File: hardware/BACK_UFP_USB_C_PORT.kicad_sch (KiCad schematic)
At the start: 30 parts, among them J7 USB4200-03-A (VIRT FLAG MOUNT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, Q18 PMOS, Q19 PMOS, Q20 PMOS, Q21 PMOS

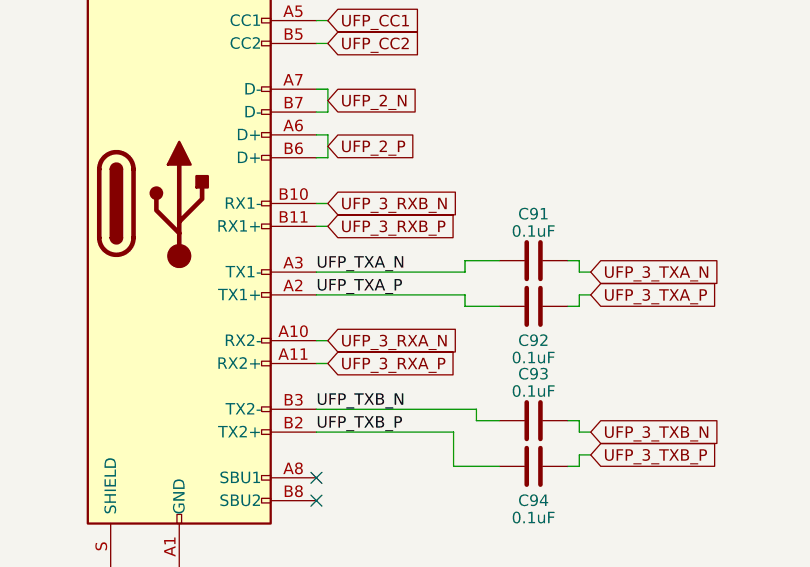
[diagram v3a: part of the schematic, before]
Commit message: working on fixing pcb impeedance
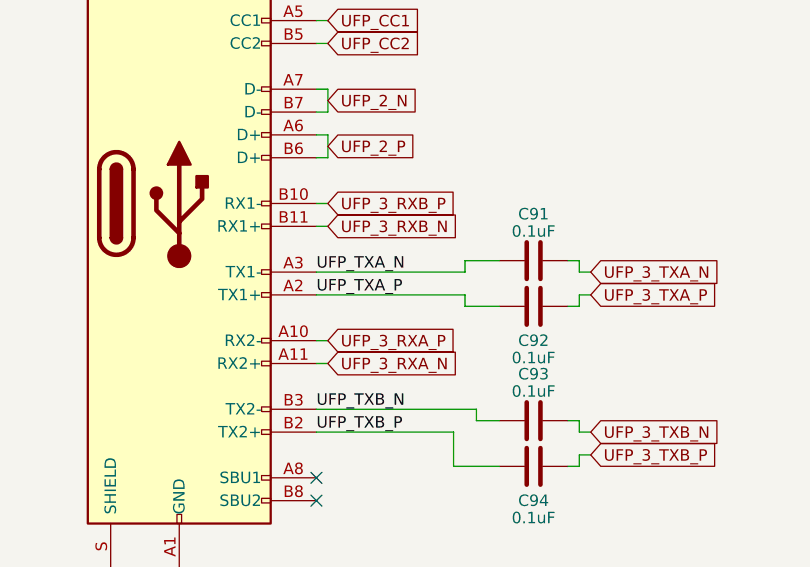
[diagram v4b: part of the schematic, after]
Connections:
- net UFP_3_RXA_N: now also J7.A11 (RX2+); no longer J7.A10 (RX2-)
- net UFP_3_RXA_P: now also J7.A10 (RX2-); no longer J7.A11 (RX2+)
- net UFP_3_RXB_N: now also J7.B11 (RX1+); no longer J7.B10 (RX1-)
- net UFP_3_RXB_P: now also J7.B10 (RX1-); no longer J7.B11 (RX1+)
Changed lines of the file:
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@@
     )
   )
-  (global_label "UFP_3_RXB_N" (shape input) (at 49.53 53.34 0) (fields_autoplaced)
+  (global_label "UFP_3_RXB_N" (shape input) (at 49.53 55.88 0) (fields_autoplaced)
     (effects (font (size 1.27 1.27)) (justify left))
-    (property "Intersheetrefs" "${INTERSHEET_REFS}" (at 65.3172 53.34 0)
+    (property "Intersheetrefs" "${INTERSHEET_REFS}" (at 65.3172 55.88 0)
       (effects (font (size 1.27 1.27)) (justify left) hide)
     )
@@
     )
   )
-  (global_label "UFP_3_RXB_P" (shape input) (at 49.53 55.88 0) (fields_autoplaced)
+  (global_label "UFP_3_RXB_P" (shape input) (at 49.53 53.34 0) (fields_autoplaced)
     (effects (font (size 1.27 1.27)) (justify left))
-    (property "Intersheetrefs" "${INTERSHEET_REFS}" (at 65.2567 55.88 0)
+    (property "Intersheetrefs" "${INTERSHEET_REFS}" (at 65.2567 53.34 0)
       (effects (font (size 1.27 1.27)) (justify left) hide)
     )
@@
     )
   )
-  (global_label "UFP_3_RXA_P" (shape input) (at 49.53 71.12 0) (fields_autoplaced)
+  (global_label "UFP_3_RXA_P" (shape input) (at 49.53 68.58 0) (fields_autoplaced)
     (effects (font (size 1.27 1.27)) (justify left))
-    (property "Intersheetrefs" "${INTERSHEET_REFS}" (at 65.0753 71.12 0)
+    (property "Intersheetrefs" "${INTERSHEET_REFS}" (at 65.0753 68.58 0)
       (effects (font (size 1.27 1.27)) (justify left) hide)
     )
@@
     )
   )
-  (global_label "UFP_3_RXA_N" (shape input) (at 49.53 68.58 0) (fields_autoplaced)
+  (global_label "UFP_3_RXA_N" (shape input) (at 49.53 71.12 0) (fields_autoplaced)
     (effects (font (size 1.27 1.27)) (justify left))
-    (property "Intersheetrefs" "${INTERSHEET_REFS}" (at 65.1358 68.58 0)
+    (property "Intersheetrefs" "${INTERSHEET_REFS}" (at 65.1358 71.12 0)
       (effects (font (size 1.27 1.27)) (justify left) hide)
     )

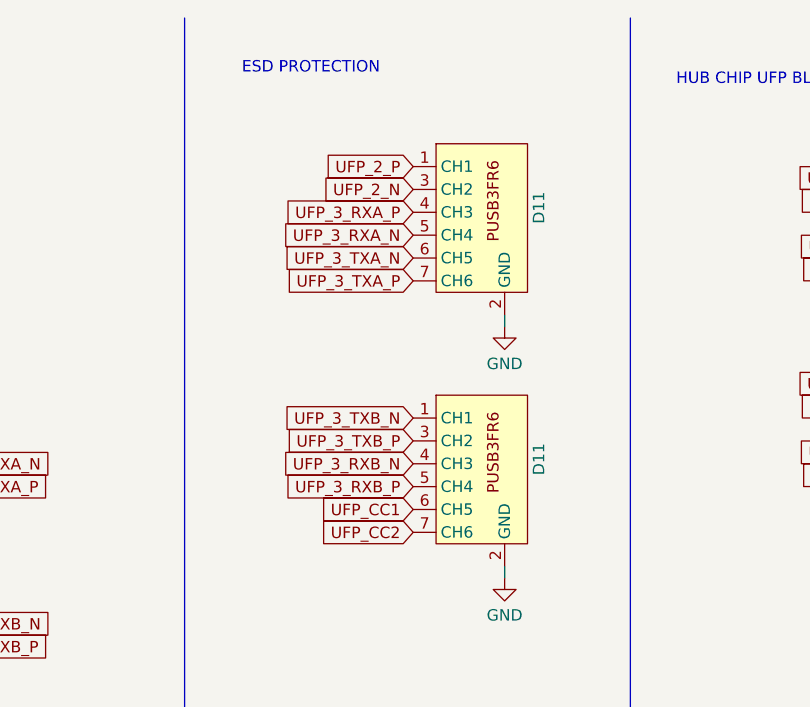
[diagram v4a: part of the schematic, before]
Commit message: fixed DP issues and finneshed overall routeing
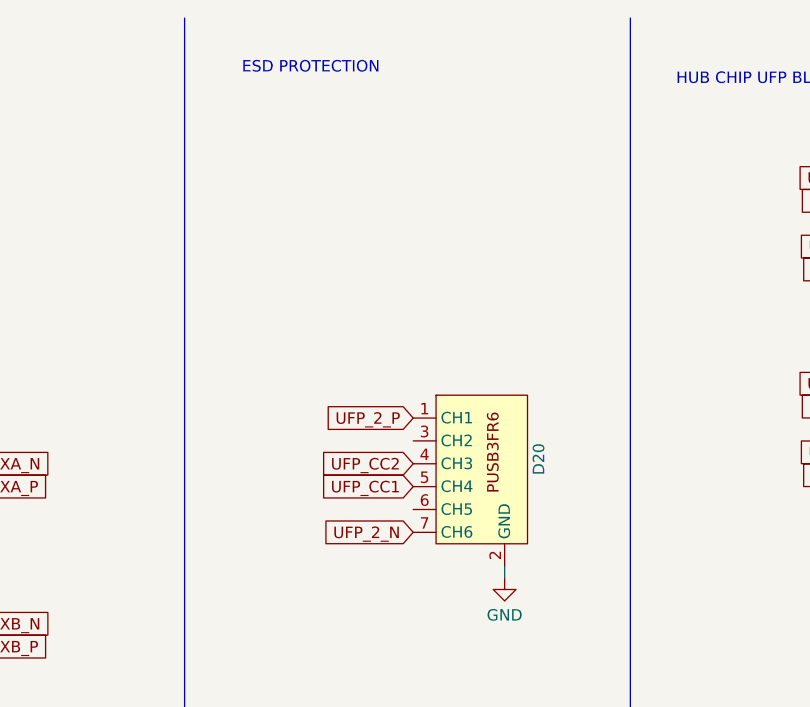
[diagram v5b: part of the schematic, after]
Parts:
- removed D11: ~, CARTHING:PUSB3AB6Z_NEX, symbol CARTHING:PUSB3FR6
- renumbered D11 to D20
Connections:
- net UFP_2_N: now also D20.7 (CH6)
- net UFP_2_P: now also D20.1 (CH1)
- net UFP_3_RXB_N: no longer D20.4 (CH3)
- net UFP_3_RXB_P: no longer D20.5 (CH4)
- net UFP_3_TXB_N: no longer D20.1 (CH1)
- net UFP_3_TXB_P: no longer D20.3 (CH2)
- net UFP_CC1: now also D20.5 (CH4); no longer D20.6 (CH5)
- net UFP_CC2: now also D20.4 (CH3); no longer D20.7 (CH6)
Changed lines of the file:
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@@
-    (stroke (width 0) (type default))
-  )
-  (wire (pts (xy 143.51 44.45) (xy 143.51 45.72))
     (stroke (width 0) (type default))
   )
@@
     (effects (font (size 1.27 1.27)) (justify left bottom))
   )
-  (global_label "UFP_3_TXB_N" (shape input) (at 133.35 55.88 180) (fields_autoplaced)
-    (effects (font (size 1.27 1.27)) (justify right))
-    (property "Intersheetrefs" "${INTERSHEET_REFS}" (at 117.8652 55.88 0)
-      (effects (font (size 1.27 1.27)) (justify right) hide)
-    )
-  )
   (global_label "UFP_2_N" (shape input) (at 49.53 41.91 0) (fields_autoplaced)
     (effects (font (size 1.27 1.27)) (justify left))
@@
     )
   )
-  (global_label "UFP_2_P" (shape input) (at 133.35 27.94 180) (fields_autoplaced)
-    (effects (font (size 1.27 1.27)) (justify right))
-    (property "Intersheetrefs" "${INTERSHEET_REFS}" (at 122.3404 27.94 0)
+  (global_label "UFP_2_P" (shape input) (at 133.35 55.88 180) (fields_autoplaced)
+    (effects (font (size 1.27 1.27)) (justify right))
+    (property "Intersheetrefs" "${INTERSHEET_REFS}" (at 122.3404 55.88 0)
       (effects (font (size 1.27 1.27)) (justify right) hide)
     )
@@
     )
   )
-  (global_label "UFP_2_N" (shape input) (at 133.35 30.48 180) (fields_autoplaced)
-    (effects (font (size 1.27 1.27)) (justify right))
-    (property "Intersheetrefs" "${INTERSHEET_REFS}" (at 122.2799 30.48 0)
+  (global_label "UFP_2_N" (shape input) (at 133.35 68.58 180) (fields_autoplaced)
+    (effects (font (size 1.27 1.27)) (justify right))
+    (property "Intersheetrefs" "${INTERSHEET_REFS}" (at 122.2799 68.58 0)
       (effects (font (size 1.27 1.27)) (justify right) hide)
     )
@@
     )
   )
-  (global_label "UFP_3_TXA_P" (shape input) (at 133.35 40.64 180) (fields_autoplaced)
-    (effects (font (size 1.27 1.27)) (justify right))
-    (property "Intersheetrefs" "${INTERSHEET_REFS}" (at 118.1071 40.64 0)
-      (effects (font (size 1.27 1.27)) (justify right) hide)
-    )
-  )
   (global_label "UFP_3_TXB_N" (shape input) (at 78.74 78.74 0) (fields_autoplaced)
     (effects (font (size 1.27 1.27)) (justify left))
@@
     )
   )
-  (global_label "UFP_3_TXB_P" (shape input) (at 133.35 58.42 180) (fields_autoplaced)
-    (effects (font (size 1.27 1.27)) (justify right))
-    (property "Intersheetrefs" "${INTERSHEET_REFS}" (at 117.9257 58.42 0)
-      (effects (font (size 1.27 1.27)) (justify right) hide)
-    )
-  )
-  (global_label "UFP_3_RXA_P" (shape input) (at 133.35 33.02 180) (fields_autoplaced)
-    (effects (font (size 1.27 1.27)) (justify right))
-    (property "Intersheetrefs" "${INTERSHEET_REFS}" (at 117.8047 33.02 0)
-      (effects (font (size 1.27 1.27)) (justify right) hide)
-    )
-  )
-  (global_label "UFP_CC1" (shape input) (at 133.35 66.04 180) (fields_autoplaced)
-    (effects (font (size 1.27 1.27)) (justify right))
-    (property "Intersheetrefs" "${INTERSHEET_REFS}" (at 122.038 66.04 0)
+  (global_label "UFP_CC1" (shape input) (at 133.35 63.5 180) (fields_autoplaced)
+    (effects (font (size 1.27 1.27)) (justify right))
+    (property "Intersheetrefs" "${INTERSHEET_REFS}" (at 122.038 63.5 0)
       (effects (font (size 1.27 1.27)) (justify right) hide)
     )
@@
     )
   )
-  (global_label "UFP_3_RXA_N" (shape input) (at 133.35 35.56 180) (fields_autoplaced)
-    (effects (font (size 1.27 1.27)) (justify right))
-    (property "Intersheetrefs" "${INTERSHEET_REFS}" (at 117.7442 35.56 0)
-      (effects (font (size 1.27 1.27)) (justify right) hide)
-    )
-  )
   (global_label "UFP_2_N" (shape input) (at 190.5 44.45 180) (fields_autoplaced)
     (effects (font (size 1.27 1.27)) (justify right))
@@
     )
   )
-  (global_label "UFP_3_TXA_N" (shape input) (at 133.35 38.1 180) (fields_autoplaced)
-    (effects (font (size 1.27 1.27)) (justify right))
-    (property "Intersheetrefs" "${INTERSHEET_REFS}" (at 118.0466 38.1 0)
-      (effects (font (size 1.27 1.27)) (justify right) hide)
-    )
-  )
   (global_label "UFP_3_RXB_P" (shape input) (at 49.53 53.34 0) (fields_autoplaced)
     (effects (font (size 1.27 1.27)) (justify left))
@@
     )
   )
-  (global_label "UFP_CC2" (shape input) (at 133.35 68.58 180) (fields_autoplaced)
-    (effects (font (size 1.27 1.27)) (justify right))
-    (property "Intersheetrefs" "${INTERSHEET_REFS}" (at 122.038 68.58 0)
+  (global_label "UFP_CC2" (shape input) (at 133.35 60.96 180) (fields_autoplaced)
+    (effects (font (size 1.27 1.27)) (justify right))
+    (property "Intersheetrefs" "${INTERSHEET_REFS}" (at 122.038 60.96 0)
       (effects (font (size 1.27 1.27)) (justify right) hide)
     )
@@
     )
   )
-  (global_label "UFP_3_RXB_N" (shape input) (at 133.35 60.96 180) (fields_autoplaced)
-    (effects (font (size 1.27 1.27)) (justify right))
-    (property "Intersheetrefs" "${INTERSHEET_REFS}" (at 117.5628 60.96 0)
-      (effects (font (size 1.27 1.27)) (justify right) hide)
-    )
-  )
   (global_label "UFP_CC_ORIENT" (shape input) (at 97.79 162.56 180) (fields_autoplaced)
     (effects (font (size 1.27 1.27)) (justify right))
@@
     (effects (font (size 1.27 1.27)) (justify right))
     (property "Intersheetrefs" "${INTERSHEET_REFS}" (at 175.1966 36.83 0)
-      (effects (font (size 1.27 1.27)) (justify right) hide)
-    )
-  )
-  (global_label "UFP_3_RXB_P" (shape input) (at 133.35 63.5 180) (fields_autoplaced)
-    (effects (font (size 1.27 1.27)) (justify right))
-    (property "Intersheetrefs" "${INTERSHEET_REFS}" (at 117.6233 63.5 0)
       (effects (font (size 1.27 1.27)) (justify right) hide)
     )
@@
         (path "/fae025e9-99c5-40c1-af6f-99dc1edbfa43/bb20a659-2b02-48fa-8ef7-389a14e86ba7"
           (reference "Q21") (unit 1)
-        )
-        (path "/fae025e9-99c5-40c1-af6f-99dc1edbfa43/ad0dde3f-c33d-40ce-8876-17a95cda421b"
-          (reference "Q22") (unit 1)
         )
       )
@@
           (reference "U13") (unit 4)
         )
-        (path "/fae025e9-99c5-40c1-af6f-99dc1edbfa43/7a7a6512-c96f-448a-bb8d-4d6e185adf7f"
-          (reference "U13") (unit 4)
-        )
       )
     )
@@
           (reference "Q19") (unit 1)
         )
-        (path "/fae025e9-99c5-40c1-af6f-99dc1edbfa43/ad0dde3f-c33d-40ce-8876-17a95cda421b"
-          (reference "Q22") (unit 1)
-        )
       )
     )
@@
   (symbol (lib_id "CARTHING:PUSB3FR6") (at 140.97 60.96 0) (unit 1)
     (in_bom yes) (on_board yes) (dnp no)
-    (property "Reference" "D11" (at 147.32 62.23 90)
+    (property "Reference" "D20" (at 147.32 62.23 90)
       (effects (font (size 1.27 1.27)) (justify left))
     )
@@
     (instances
       (project "usbc-car-module"
-        (path "/fae025e9-99c5-40c1-af6f-99dc1edbfa43/fe8e7353-13b3-4aa6-97f7-d88e32d23b04"
-          (reference "D11") (unit 1)
-        )
         (path "/fae025e9-99c5-40c1-af6f-99dc1edbfa43/bb20a659-2b02-48fa-8ef7-389a14e86ba7"
           (reference "D20") (unit 1)
@@
           (reference "Q20") (unit 1)
         )
-        (path "/fae025e9-99c5-40c1-af6f-99dc1edbfa43/ad0dde3f-c33d-40ce-8876-17a95cda421b"
-          (reference "Q22") (unit 1)
-        )
       )
     )
@@
         (path "/fae025e9-99c5-40c1-af6f-99dc1edbfa43/bb20a659-2b02-48fa-8ef7-389a14e86ba7"
           (reference "#PWR0106") (unit 1)
-        )
-      )
-    )
-  )
-  (symbol (lib_id "CARTHING:PUSB3FR6") (at 140.97 33.02 0) (unit 1)
-    (in_bom yes) (on_board yes) (dnp no)
-    (property "Reference" "D11" (at 147.32 34.29 90)
-      (effects (font (size 1.27 1.27)) (justify left))
-    )
-    (property "Value" "~" (at 134.62 15.24 0)
-      (effects (font (size 1.27 1.27)))
-    )
-    (property "Footprint" "CARTHING:PUSB3AB6Z_NEX" (at 134.62 15.24 0)
-      (effects (font (size 1.27 1.27)) hide)
-    )
-    (property "Datasheet" "" (at 134.62 15.24 0)
-      (effects (font (size 1.27 1.27)) hide)
-    )
-    (pin "1")
-    (pin "2")
-    (pin "3")
-    (pin "4")
-    (pin "5")
-    (pin "6")
-    (pin "7")
-    (instances
-      (project "usbc-car-module"
-        (path "/fae025e9-99c5-40c1-af6f-99dc1edbfa43/fe8e7353-13b3-4aa6-97f7-d88e32d23b04"
-          (reference "D11") (unit 1)
-        )
-        (path "/fae025e9-99c5-40c1-af6f-99dc1edbfa43/bb20a659-2b02-48fa-8ef7-389a14e86ba7"
-          (reference "D19") (unit 1)
         )
       )
@@
           (reference "Q18") (unit 1)
         )
-        (path "/fae025e9-99c5-40c1-af6f-99dc1edbfa43/ad0dde3f-c33d-40ce-8876-17a95cda421b"
-          (reference "Q22") (unit 1)
-        )
       )
     )
@@
         )
       )
-    )
-  )
-  (symbol (lib_id "power:GND") (at 143.51 45.72 0) (unit 1)
-    (in_bom yes) (on_board yes) (dnp no) (fields_autoplaced)
-    (property "Reference" "#PWR0116" (at 143.51 52.07 0)
-      (effects (font (size 1.27 1.27)) hide)
-    )
-    (property "Value" "GND" (at 143.51 49.8555 0)
-      (effects (font (size 1.27 1.27)))
-    )
-    (property "Footprint" "" (at 143.51 45.72 0)
-      (effects (font (size 1.27 1.27)) hide)
-    )
-    (property "Datasheet" "" (at 143.51 45.72 0)
-      (effects (font (size 1.27 1.27)) hide)
-    )
-    (pin "1")
-    (instances
-      (project "usbc-car-module"
-        (path "/fae025e9-99c5-40c1-af6f-99dc1edbfa43/bb20a659-2b02-48fa-8ef7-389a14e86ba7"
-          (reference "#PWR0116") (unit 1)
-        )
-      )

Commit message: minor revisions
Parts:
- D20: value ~ -> PUSB3AB6Z
- Q18, Q19, Q20, Q21: value PMOS -> PMPB09R5VPX
- U13: value ~ -> USB5926C
- U15: value ~ -> PTN5100BMSP
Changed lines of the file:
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@@
       (effects (font (size 1.27 1.27)))
     )
-    (property "Value" "PMOS" (at 198.12 137.9761 90)
+    (property "Value" "PMPB09R5VPX" (at 198.12 137.9761 90)
       (effects (font (size 1.27 1.27)))
     )
@@
       (effects (font (size 1.27 1.27)))
     )
-    (property "Value" "~" (at 231.14 85.09 0)
+    (property "Value" "USB5926C" (at 245.11 25.4 0)
       (effects (font (size 1.27 1.27)))
     )
@@
       (effects (font (size 1.27 1.27)))
     )
-    (property "Value" "PMOS" (at 180.34 112.5761 90)
+    (property "Value" "PMPB09R5VPX" (at 180.34 112.5761 90)
       (effects (font (size 1.27 1.27)))
     )
@@
       (effects (font (size 1.27 1.27)) (justify left))
     )
-    (property "Value" "~" (at 134.62 43.18 0)
+    (property "Value" "PUSB3AB6Z" (at 140.97 50.8 0)
       (effects (font (size 1.27 1.27)))
     )
@@
       (effects (font (size 1.27 1.27)) (justify left))
     )
-    (property "Value" "~" (at 96.52 127 0)
+    (property "Value" "PTN5100BMSP" (at 96.52 127 0)
       (effects (font (size 1.27 1.27)))
     )
@@
       (effects (font (size 1.27 1.27)))
     )
-    (property "Value" "PMOS" (at 198.12 112.5761 90)
+    (property "Value" "PMPB09R5VPX" (at 198.12 112.5761 90)
       (effects (font (size 1.27 1.27)))
     )
@@
       (effects (font (size 1.27 1.27)))
     )
-    (property "Value" "PMOS" (at 180.34 137.9761 90)
-      (effects (font (size 1.27 1.27)))
-    )
+    (property "Value" "PMPB09R5VPX" (at 180.34 137.9761 90)
+      (effects (font (size 1.27 1.27)))
+    )

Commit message: working on complie issues
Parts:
- added JP21: ~, Jumper:SolderJumper-2_P1.3mm_Open_RoundedPad1.0x1.5mm, symbol Jumper:SolderJumper_2_Open
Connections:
- net UFP_CC_ORIENT: now also JP21.2 (B); no longer U15.9 (CC_ORIENT)
- new net: JP21.1 (A), U15.9 (CC_ORIENT)
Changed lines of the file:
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@@
+    (stroke (width 0) (type default))
+  )
+  (wire (pts (xy 82.55 162.56) (xy 97.79 162.56))
     (stroke (width 0) (type default))
   )
@@
     )
   )
-  (global_label "UFP_CC_ORIENT" (shape input) (at 97.79 162.56 180) (fields_autoplaced)
-    (effects (font (size 1.27 1.27)) (justify right))
-    (property "Intersheetrefs" "${INTERSHEET_REFS}" (at 80.0675 162.56 0)
+  (global_label "UFP_CC_ORIENT" (shape input) (at 74.93 162.56 180) (fields_autoplaced)
+    (effects (font (size 1.27 1.27)) (justify right))
+    (property "Intersheetrefs" "${INTERSHEET_REFS}" (at 57.2075 162.56 0)
       (effects (font (size 1.27 1.27)) (justify right) hide)
     )
@@
         )
       )
+    )
+  )
+  (symbol (lib_id "Jumper:SolderJumper_2_Open") (at 78.74 162.56 180) (unit 1)
+    (in_bom yes) (on_board yes) (dnp no) (fields_autoplaced)
+    (property "Reference" "JP21" (at 78.74 160.5821 0)
+      (effects (font (size 1.27 1.27)))
+    )
+    (property "Value" "~" (at 80.0173 160.909 90)
+      (effects (font (size 1.27 1.27)) (justify right))
+    )
+    (property "Footprint" "Jumper:SolderJumper-2_P1.3mm_Open_RoundedPad1.0x1.5mm" (at 78.74 162.56 0)
+      (effects (font (size 1.27 1.27)) hide)
+    )
+    (property "Datasheet" "~" (at 78.74 162.56 0)
+      (effects (font (size 1.27 1.27)) hide)
+    )
+    (pin "1")
+    (pin "2")
+    (instances
+      (project "usbc-car-module"
+        (path "/fae025e9-99c5-40c1-af6f-99dc1edbfa43/bb20a659-2b02-48fa-8ef7-389a14e86ba7"
+          (reference "JP21") (unit 1)
+        )
+      )
